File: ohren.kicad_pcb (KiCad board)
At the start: 2 copper layers, 60 x 28.7 mm, 0 parts

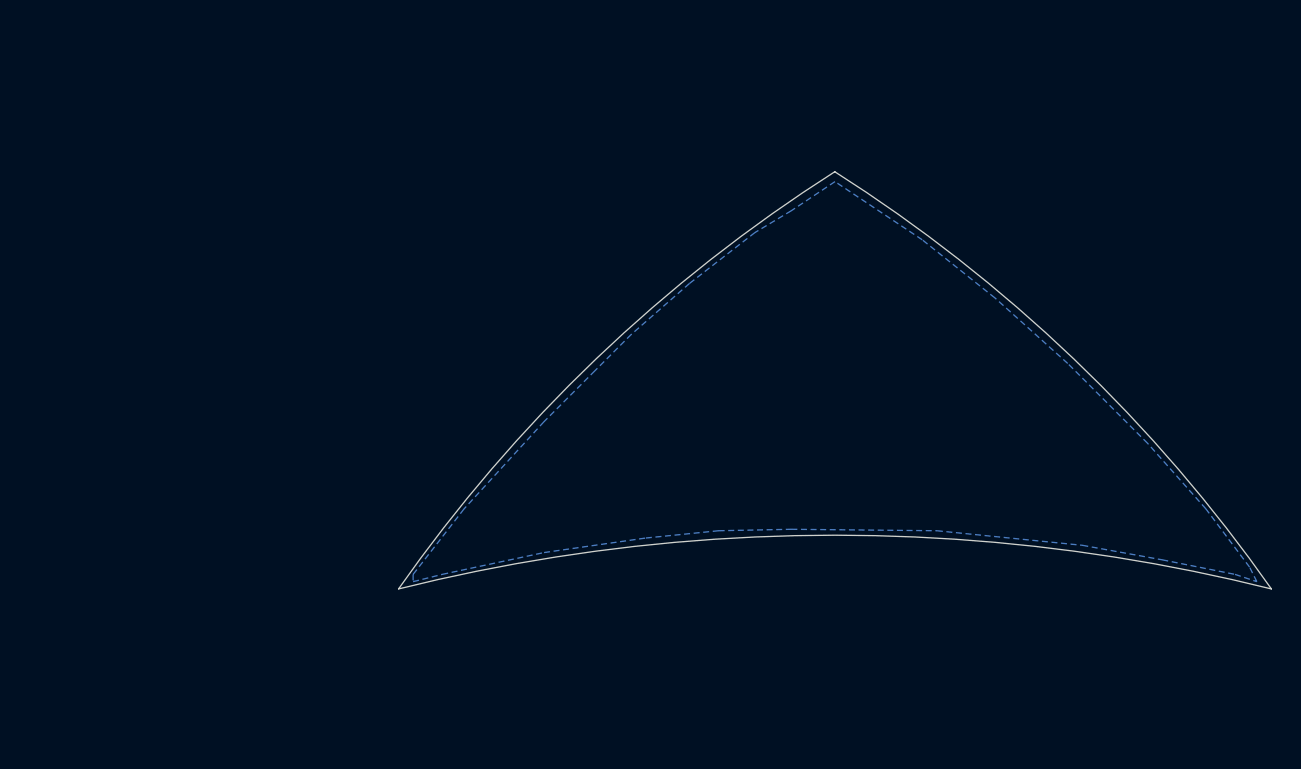
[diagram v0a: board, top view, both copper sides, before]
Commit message: Add LEDs and drivers
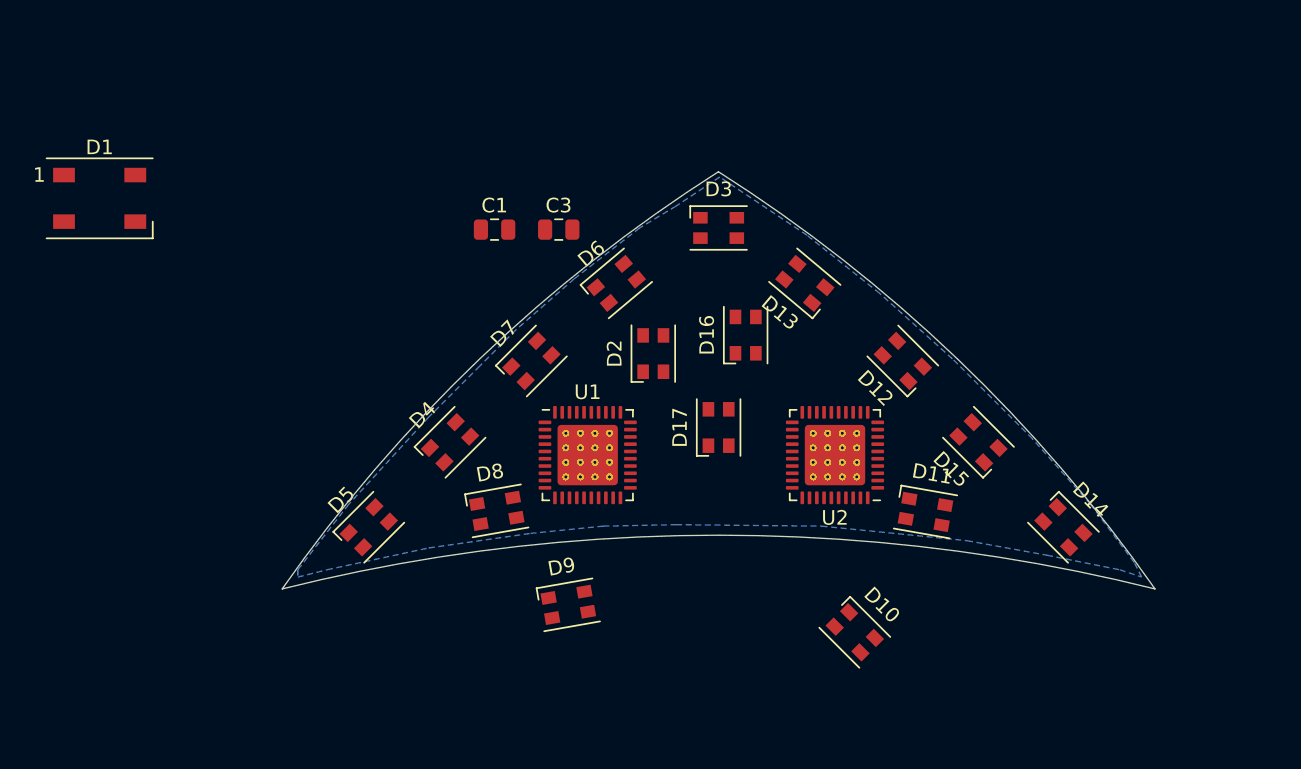
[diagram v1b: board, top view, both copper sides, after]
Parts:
- added C1: C, Capacitor_SMD:C_0805_2012Metric, F.Cu at (124.6, 91.3)
- added C3: C, Capacitor_SMD:C_0805_2012Metric, F.Cu at (129.0, 91.3)
- added D1: WS2812B, LED_SMD:LED_WS2812B_PLCC4_5.0x5.0mm_P3.2mm, F.Cu at (97.5, 89.2)
- added D10: LED_ARGB, LED_SMD:LED_Cree-PLCC4_3.2x2.8mm_CCW, F.Cu at (149.4, 119.0)
- added D11: LED_ARGB, LED_SMD:LED_Cree-PLCC4_3.2x2.8mm_CCW, F.Cu at (154.2, 110.7)
- added D12: LED_ARGB, LED_SMD:LED_Cree-PLCC4_3.2x2.8mm_CCW, F.Cu at (152.7, 100.3)
- added D13: LED_ARGB, LED_SMD:LED_Cree-PLCC4_3.2x2.8mm_CCW, F.Cu at (145.9, 95.0)
- added D14: LED_ARGB, LED_SMD:LED_Cree-PLCC4_3.2x2.8mm_CCW, F.Cu at (163.7, 111.8)
- added D15: LED_ARGB, LED_SMD:LED_Cree-PLCC4_3.2x2.8mm_CCW, F.Cu at (157.9, 105.9)
- added D16: LED_ARGB, LED_SMD:LED_Cree-PLCC4_3.2x2.8mm_CCW, F.Cu at (141.9, 98.6)
- added D17: LED_ARGB, LED_SMD:LED_Cree-PLCC4_3.2x2.8mm_CCW, F.Cu at (140.0, 104.9)
- added D2: LED_ARGB, LED_SMD:LED_Cree-PLCC4_3.2x2.8mm_CCW, F.Cu at (135.5, 99.8)
- added D3: LED_ARGB, LED_SMD:LED_Cree-PLCC4_3.2x2.8mm_CCW, F.Cu at (140.0, 91.2)
- added D4: LED_ARGB, LED_SMD:LED_Cree-PLCC4_3.2x2.8mm_CCW, F.Cu at (121.5, 105.9)
- added D5: LED_ARGB, LED_SMD:LED_Cree-PLCC4_3.2x2.8mm_CCW, F.Cu at (116.0, 111.8)
- added D6: LED_ARGB, LED_SMD:LED_Cree-PLCC4_3.2x2.8mm_CCW, F.Cu at (133.0, 95.0)
- added D7: LED_ARGB, LED_SMD:LED_Cree-PLCC4_3.2x2.8mm_CCW, F.Cu at (127.1, 100.3)
- added D8: LED_ARGB, LED_SMD:LED_Cree-PLCC4_3.2x2.8mm_CCW, F.Cu at (124.7, 110.6)
- added D9: LED_ARGB, LED_SMD:LED_Cree-PLCC4_3.2x2.8mm_CCW, F.Cu at (129.7, 117.1)
- added U1: TLC5951RHA, Package_DFN_QFN:Texas_S-PVQFN-N40_EP4.15x4.15mm_ThermalVias, F.Cu at (131.0, 106.8)
- added U2: TLC5951RHA, Package_DFN_QFN:Texas_S-PVQFN-N40_EP4.15x4.15mm_ThermalVias, F.Cu at (148.0, 106.8)
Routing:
- added copper zone on B.Cu, net GND
- removed copper zone on B.Cu, net (none)
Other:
- rule trace_min: 0.2 -> 0.127
- rule via_min_size: 0.4 -> 0.3

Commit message: Route (sort of) clock and data bus
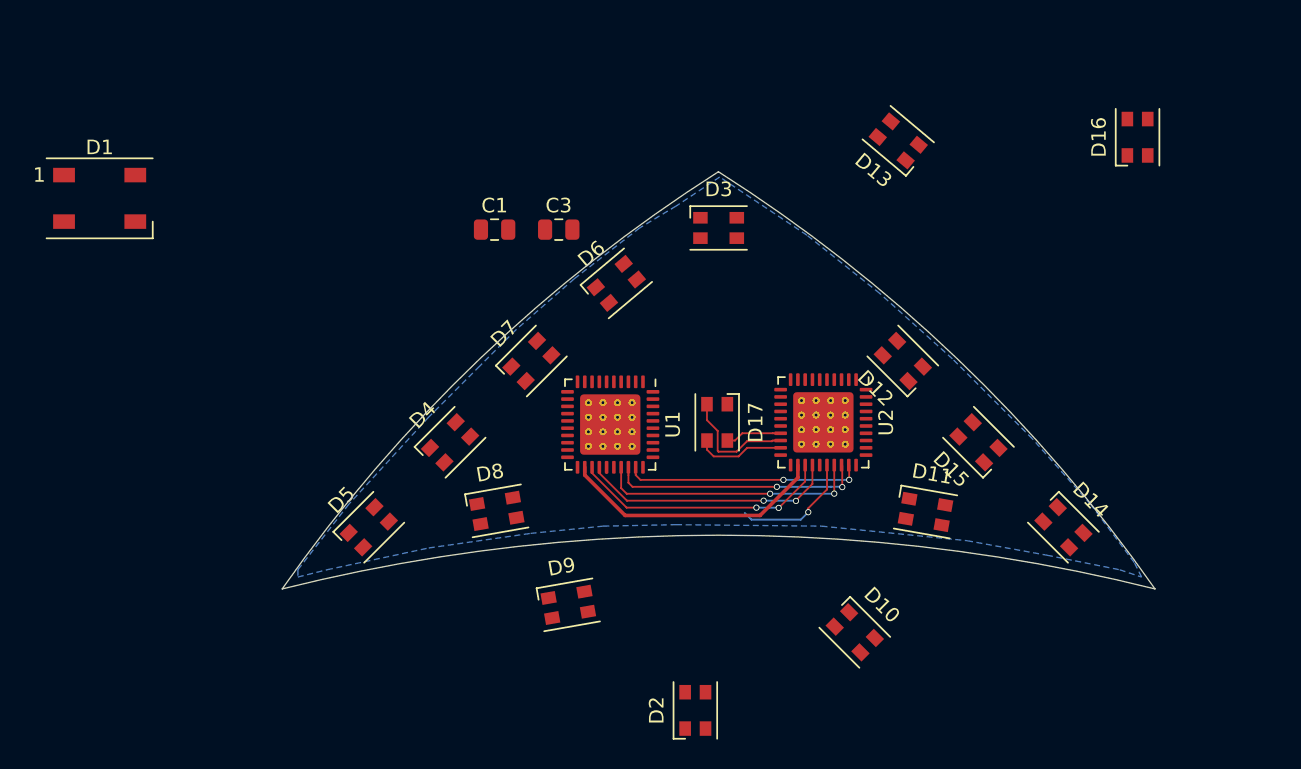
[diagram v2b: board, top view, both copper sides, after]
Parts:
- moved D16 30.2 mm to (168.8, 85.0)
- moved D2 24.7 mm to (138.4, 124.3)
- moved D13 11.7 mm to (152.3, 85.2)
- moved U1 2.61 mm to (132.6, 104.7), turned to 270 degrees
- moved U2 2.39 mm to (147.2, 104.5), turned to 270 degrees
- moved D17 0.37 mm to (139.9, 104.5), turned to 270 degrees
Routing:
- net VDD: track 0.00 -> 18.3 mm
- net /GSSCK: track 0.00 -> 18.2 mm, vias 0 -> 2
- net /XBLINK: track 0.00 -> 17.9 mm, vias 0 -> 2
- net /DCSCK: track 0.00 -> 17.6 mm, vias 0 -> 2
- net /GSLAT: track 0.00 -> 17.4 mm, vias 0 -> 2
- net /GSCKG: track 0.00 -> 16.4 mm, vias 0 -> 2
- net /GSSCHAIN: track 0.00 -> 8.54 mm, vias 0 -> 1
- net /U2_R7: track 0.00 -> 8.18 mm
- net /U2_G7: track 0.00 -> 6.13 mm
- net /U2_B7: track 0.00 -> 3.87 mm

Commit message: Route
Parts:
- added C5: C, Capacitor_SMD:C_1210_3225Metric, B.Cu at (122.3, 105.9)
- added C6: C, Capacitor_SMD:C_1210_3225Metric, B.Cu at (147.3, 97.7)
- added C7: C, Capacitor_SMD:C_1210_3225Metric, B.Cu at (130.7, 97.7)
- added C8: C, Capacitor_SMD:C_1210_3225Metric, B.Cu at (156.5, 108.0)
- added J1: Conn_01x14_Male, catear-pcb:solder_conn14, B.Cu at (137.3, 112.1)
- C1, C3: moved to B.Cu
- moved D2 40.9 mm to (129.8, 84.3)
- moved D16 31.5 mm to (140.0, 97.7)
- moved C1 24.7 mm to (145.1, 105.0)
- moved C3 15.8 mm to (131.3, 106.9), turned to 90 degrees
- moved D3 10.6 mm to (143.6, 81.2)
- moved D14 10.3 mm to (156.9, 104.0)
- moved D10 10.1 mm to (154.8, 110.5), turned to 350 degrees
- moved D15 9.65 mm to (151.4, 98.8), turned to 140 degrees
- moved D11 9.43 mm to (163.6, 111.2), turned to 315 degrees
- moved D5 9.13 mm to (122.2, 105.1)
- moved D12 8.99 mm to (145.9, 94.3), turned to 145 degrees
- moved D8 8.32 mm to (116.5, 111.2), turned to 45 degrees
- moved D4 8.19 mm to (127.3, 100.1)
- moved D6 8.15 mm to (140.2, 91.2), turned to 0 degrees
- moved D7 8.10 mm to (133.4, 95.2)
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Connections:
- net /XBLINK renamed /XBLNK
- U1 pad 25: Net-(U1-Pad25) -> /DCSIN
- U1 pad 26: Net-(U1-Pad26) -> /GSSIN
- U1 pad 29: /GSCKG -> /GSCKB
- U1 pad 30: /GSCKR -> /GSCKB
- U2 pad 29: /GSCKG -> /GSCKB
- U2 pad 30: /GSCKR -> /GSCKB
- U2 pad 5: Net-(U2-Pad5) -> /GSSOUT
- U2 pad 6: Net-(U2-Pad6) -> /DCSOUT
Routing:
- net VCC: track 0.00 -> 124.9 mm, vias 0 -> 9
- net /GSCKB: track 0.00 -> 32.3 mm, vias 0 -> 2
- net /DCSCHAIN: track 0.00 -> 27.3 mm, vias 0 -> 2
- net /GSSOUT: track 0.00 -> 20.0 mm, vias 0 -> 1
- net /U2_G1: track 0.00 -> 18.8 mm
- net /GSSCHAIN: track 8.54 -> 27.1 mm, vias 1 -> 2
- net /DCSOUT: track 0.00 -> 18.3 mm, vias 0 -> 1
- net /U2_B1: track 0.00 -> 18.1 mm
- net /U1_R6: track 0.00 -> 17.5 mm
- net /GSCKG: track 16.4 -> 0.00 mm, vias 2 -> 0
- net /U1_B2: track 0.00 -> 16.4 mm, vias 0 -> 2
- net /U1_G2: track 0.00 -> 15.3 mm, vias 0 -> 2
- net /U1_B6: track 0.00 -> 15.2 mm
- net /U2_R1: track 0.00 -> 14.8 mm
- net /U1_G6: track 0.00 -> 14.2 mm
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- added copper zone on F.Cu, net VCC

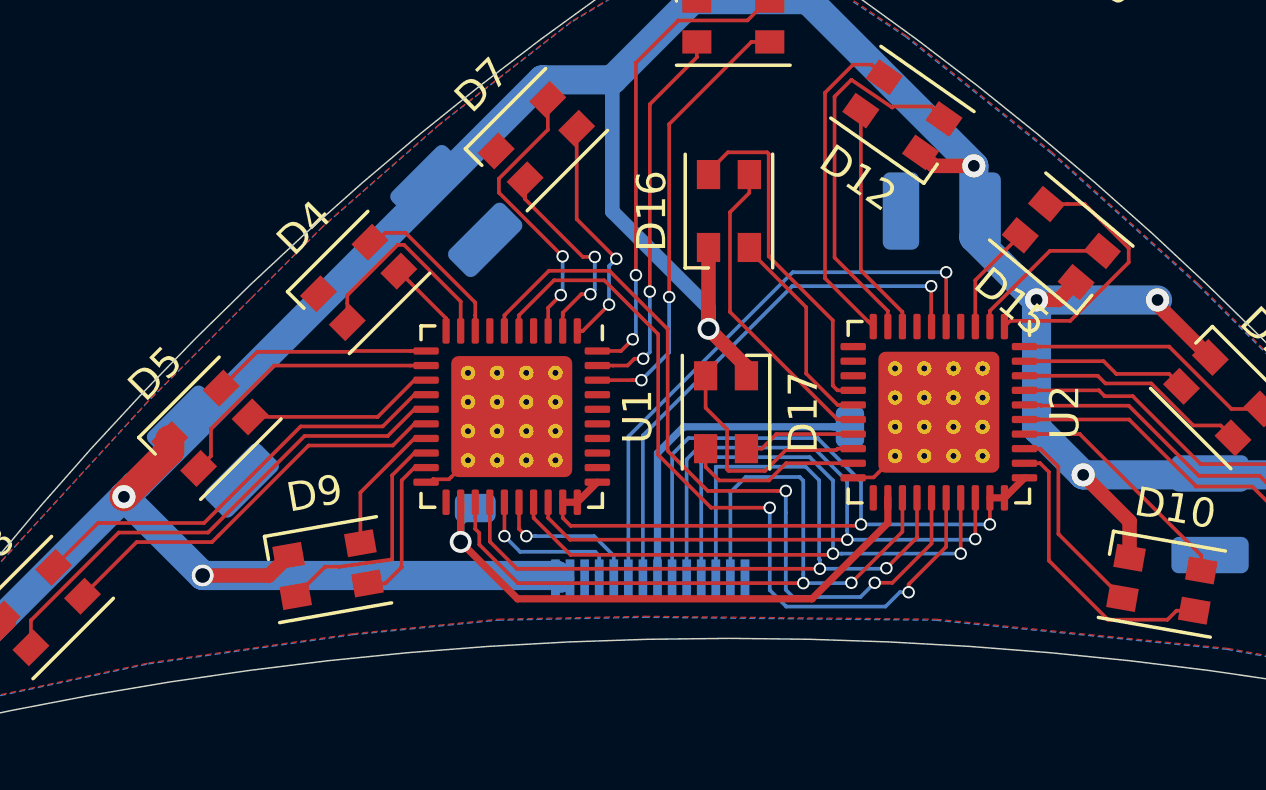
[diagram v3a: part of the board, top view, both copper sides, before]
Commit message: Add some bypass capacitance
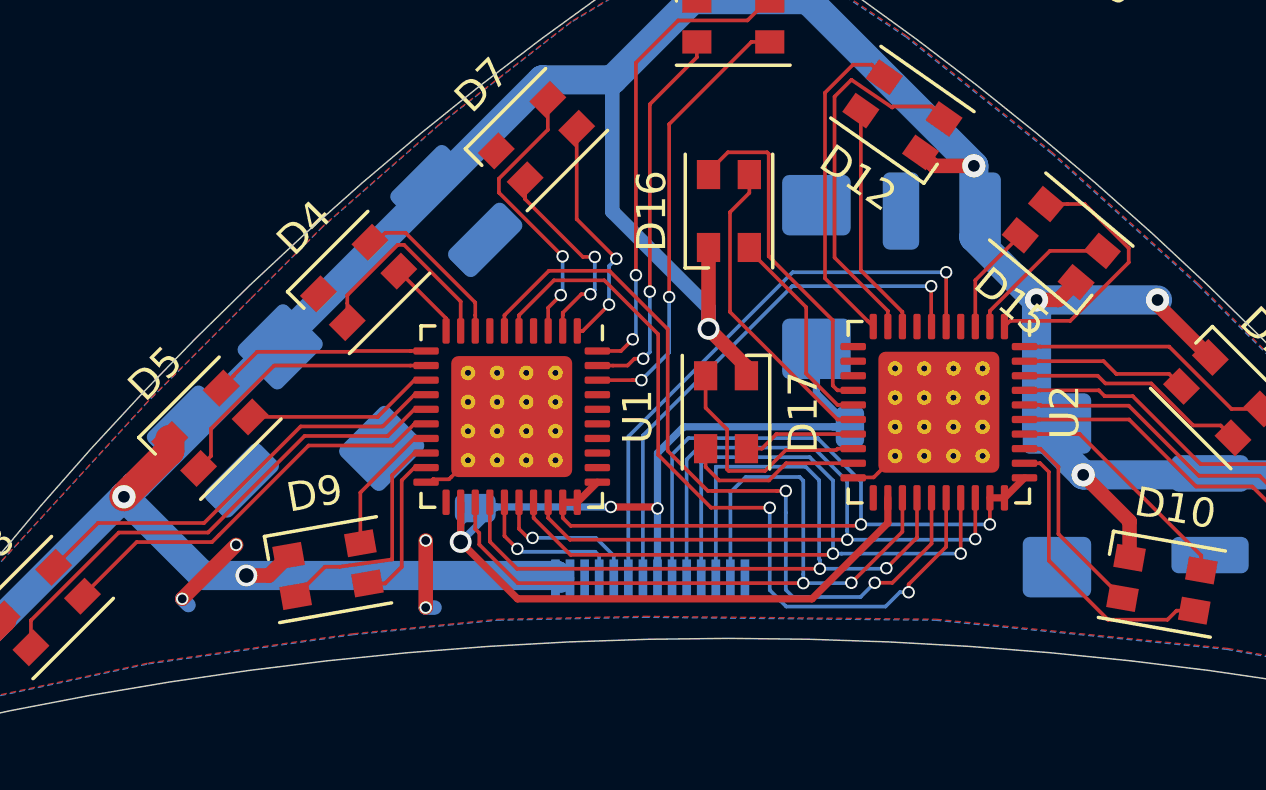
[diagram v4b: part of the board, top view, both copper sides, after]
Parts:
- added C10: CP, Capacitor_Tantalum_SMD:CP_EIA-6032-28_Kemet-C, B.Cu at (151.2, 107.4)
- added C4: CP, Capacitor_Tantalum_SMD:CP_EIA-6032-28_Kemet-C, B.Cu at (143.0, 99.9)
- added C9: CP, Capacitor_Tantalum_SMD:CP_EIA-6032-28_Kemet-C, B.Cu at (126.3, 104.0)
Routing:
- net VDD: track 32.0 -> 42.4 mm, vias 1 -> 3
- net (no net): track 0.00 -> 5.52 mm, vias 0 -> 4
- net VCC: track 124.9 -> 123.4 mm

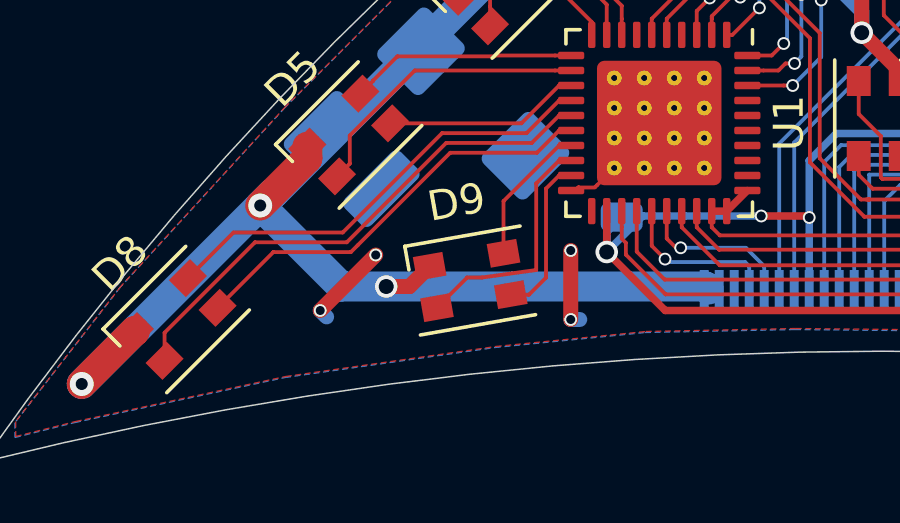
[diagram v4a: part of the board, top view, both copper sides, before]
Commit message: Add GND supports to GND net
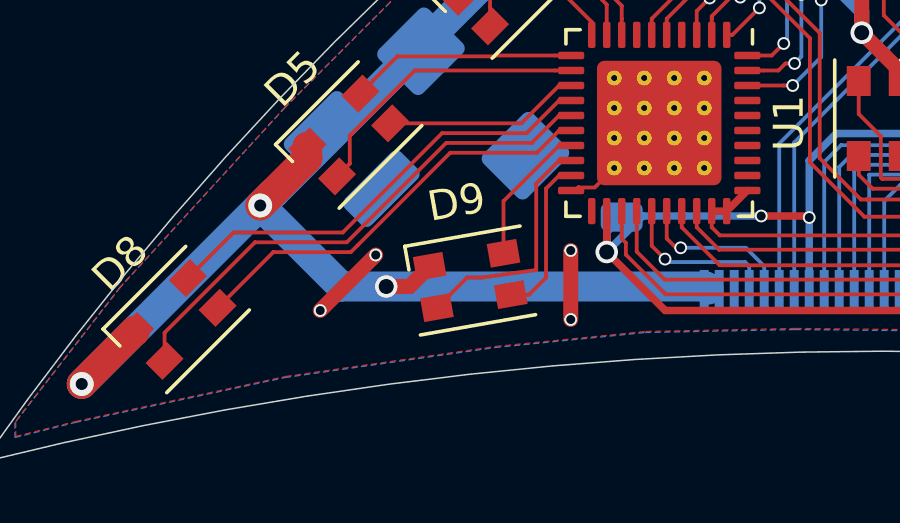
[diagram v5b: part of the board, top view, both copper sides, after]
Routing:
- net (no net): track 5.52 -> 0.00 mm, vias 4 -> 0
- net GND: track 7.74 -> 12.7 mm, vias 0 -> 4
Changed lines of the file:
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@@
     (thickness 1.6)
     (drawings 3)
-    (tracks 478)
+    (tracks 476)
     (zones 0)
     (modules 29)
@@
   (gr_arc (start 83 177) (end 170 116) (angle -22.52944362) (layer Edge.Cuts) (width 0.05))
   (gr_arc (start 140 236) (end 170 116) (angle -28.07248694) (layer Edge.Cuts) (width 0.05))
-  (via (at 129.6 108.95) (size 0.427) (drill 0.3) (layers F.Cu B.Cu) (net 0))
-  (via (at 129.6 111.25) (size 0.427) (drill 0.3) (layers F.Cu B.Cu) (net 0))
-  (segment (start 129.6 108.95) (end 129.6 111.25) (width 0.5) (layer F.Cu) (net 0))
-  (segment (start 129.6 111.25) (end 129.901934 111.25) (width 0.5) (layer B.Cu) (net 0))
-  (via (at 123.1 109.1) (size 0.427) (drill 0.3) (layers F.Cu B.Cu) (net 0))
-  (via (at 121.25 110.95) (size 0.427) (drill 0.3) (layers F.Cu B.Cu) (net 0))
-  (segment (start 123.1 109.1) (end 121.25 110.95) (width 0.5) (layer F.Cu) (net 0))
-  (segment (start 121.25 110.95) (end 121.463499 111.163499) (width 0.5) (layer B.Cu) (net 0))
+  (via (at 129.6 108.95) (size 0.427) (drill 0.3) (layers F.Cu B.Cu) (net 37))
+  (via (at 129.6 111.25) (size 0.427) (drill 0.3) (layers F.Cu B.Cu) (net 37))
+  (segment (start 129.6 108.95) (end 129.6 111.25) (width 0.5) (layer F.Cu) (net 37))
+  (via (at 123.1 109.1) (size 0.427) (drill 0.3) (layers F.Cu B.Cu) (net 37))
+  (via (at 121.25 110.95) (size 0.427) (drill 0.3) (layers F.Cu B.Cu) (net 37))
+  (segment (start 123.1 109.1) (end 121.25 110.95) (width 0.5) (layer F.Cu) (net 37))
   (via (at 150.55 100.7) (size 0.8) (drill 0.4) (layers F.Cu B.Cu) (net 14))
   (segment (start 150.5 100.65) (end 150.55 100.7) (width 0.127) (layer F.Cu) (net 14))

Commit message: Partial reroute
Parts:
- removed D1: WS2812B, LED_SMD:LED_WS2812B_PLCC4_5.0x5.0mm_P3.2mm
- removed D13, D16, D2, D3: LED_ARGB, LED_SMD:LED_Cree-PLCC4_3.2x2.8mm_CCW
- added D19: LED, catear-pcb:smd_led_universal, F.Cu at (155.1, 103.1)
- added D20: LED, catear-pcb:smd_led_universal, F.Cu at (160.5, 108.7)
- added D21: LED, catear-pcb:smd_led_universal, F.Cu at (149.5, 97.8)
- added D22: LED, catear-pcb:smd_led_universal, F.Cu at (136.3, 93.2)
- added D23: LED, catear-pcb:smd_led_universal, F.Cu at (143.7, 93.2)
- added D24: LED, catear-pcb:smd_led_universal, F.Cu at (130.6, 97.8)
- added D25: LED, catear-pcb:smd_led_universal, F.Cu at (119.6, 108.7)
- added D26: LED, catear-pcb:smd_led_universal, F.Cu at (125.0, 103.1)
- added R1: 2k4, Resistor_SMD:R_0402_1005Metric, F.Cu at (135.9, 108.4)
- added R2: 2k4, Resistor_SMD:R_0402_1005Metric, B.Cu at (142.4, 108.4)
- J1: moved to F.Cu
- U2: moved to B.Cu
- moved C1 30.2 mm to (175.1, 101.7)
- moved C4 29.1 mm to (171.2, 92.7)
- moved C10 23.3 mm to (165.6, 89.1)
- moved C3 21.2 mm to (112.2, 97.7)
- moved C9 16.4 mm to (116.7, 90.8)
- moved C6 12.5 mm to (159.1, 93.5)
- moved C8 11.2 mm to (164.6, 100.2)
- moved C5 8.04 mm to (114.9, 102.7)
- moved C7 7.51 mm to (125.1, 92.6)
- moved D17 6.76 mm to (140.0, 97.8)
- moved J1 4.01 mm to (138.7, 108.4)
- moved U2 2.08 mm to (145.2, 104.2), turned to 180 degrees
- moved D14 1.93 mm to (158.2, 105.5)
- moved D15 1.87 mm to (152.7, 100.1), turned to 135 degrees
- moved D12 1.12 mm to (146.8, 95.0), turned to 320 degrees
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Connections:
- D10 pad 2: /U2_R0 -> /U2_R7
- D10 pad 3: /U2_G0 -> /U2_G7
- D10 pad 4: /U2_B0 -> /U2_B7
- D11 pad 2: /U2_R1 -> /U2_R6
- D11 pad 3: /U2_G1 -> /U2_G6
- D11 pad 4: /U2_B1 -> /U2_B6
- D12 pad 2: /U2_R4 -> /U2_R2
- D12 pad 3: /U2_G4 -> /U2_G2
- D12 pad 4: /U2_B4 -> /U2_B2
- D14 pad 2: /U2_R2 -> /U2_R5
- D14 pad 3: /U2_G2 -> /U2_G5
- D14 pad 4: /U2_B2 -> /U2_B5
- D17 pad 2: /U2_R7 -> /U2_R0
- D17 pad 3: /U2_G7 -> /U2_G0
- D17 pad 4: /U2_B7 -> /U2_B0
- D4 pad 2: /U1_R4 -> /U1_R3
- D4 pad 3: /U1_G4 -> /U1_G3
- D4 pad 4: /U1_B4 -> /U1_B3
- D6 pad 2: /U1_R2 -> /U1_R0
- D6 pad 3: /U1_G2 -> /U1_G0
- D6 pad 4: /U1_B2 -> /U1_B0
- D7 pad 2: /U1_R3 -> /U1_R1
- D7 pad 3: /U1_G3 -> /U1_G1
- D7 pad 4: /U1_B3 -> /U1_B1
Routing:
- net VCC: track 123.4 -> 0.00 mm, vias 9 -> 0
- net (no net): track 0.00 -> 82.9 mm, vias 0 -> 4
- net VDD: track 42.4 -> 6.66 mm, vias 3 -> 1
- net /DCSCK: track 29.2 -> 6.46 mm, vias 2 -> 1
- net /GSCKB: track 32.3 -> 9.77 mm, vias 2 -> 1
- net /GSSCK: track 29.0 -> 6.63 mm, vias 2 -> 1
- net /XBLNK: track 28.6 -> 6.56 mm, vias 2 -> 1
- net /GSLAT: track 29.2 -> 7.17 mm, vias 2 -> 1
- net /GSSOUT: track 20.0 -> 0.00 mm, vias 1 -> 0
- net /U2_G1: track 18.8 -> 0.00 mm
- net /DCSOUT: track 18.3 -> 0.00 mm, vias 1 -> 0
- net /U2_B1: track 18.1 -> 0.00 mm
- net /U1_B2: track 16.4 -> 0.00 mm, vias 2 -> 0
- net /U1_B0: track 0.00 -> 15.7 mm
- net /U2_R1: track 14.8 -> 0.00 mm
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- added copper zone on F.Cu, net GND
- removed copper zone on F.Cu, net VCC
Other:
- net class Default: trace_width 0.25 -> 0.127; via_dia 0.8 -> 0.6; via_drill 0.4 -> 0.3
- rule via_min_size: 0.3 -> 0.6
